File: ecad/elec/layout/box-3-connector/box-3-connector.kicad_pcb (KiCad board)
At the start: 2 copper layers, 72.5 x 7.9 mm, 2 parts

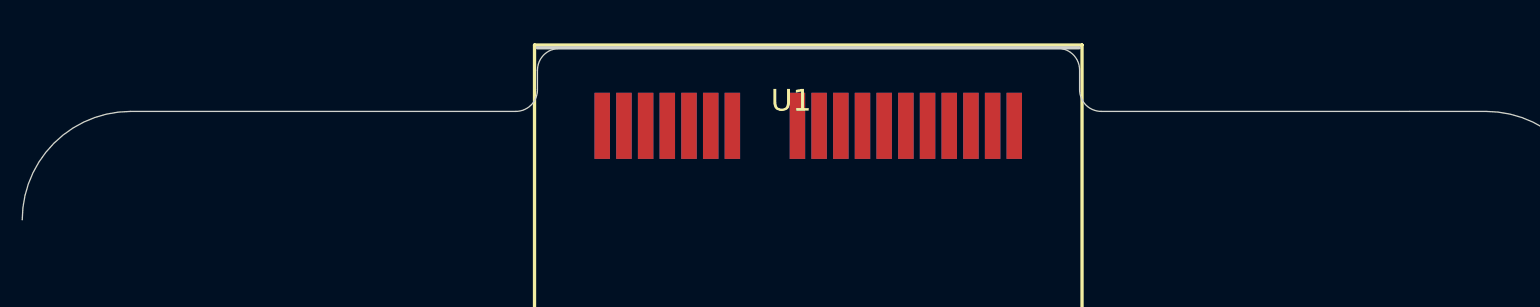
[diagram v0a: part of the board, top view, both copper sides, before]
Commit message: remove default and start fleshing out layouts. fixed issue with fab extending beyond edge cuts in box-3-connector footprint (CONN_5_)
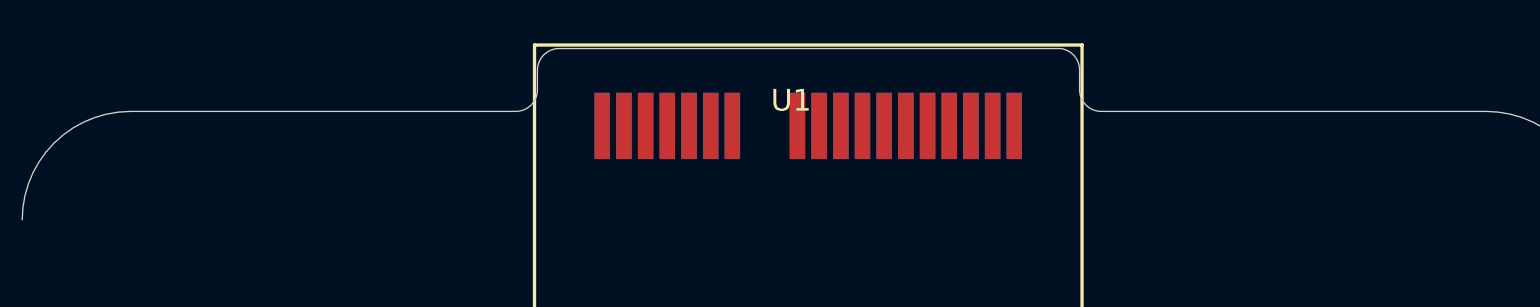
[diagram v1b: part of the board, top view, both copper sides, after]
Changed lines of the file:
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@@
         (effects (font (size 1 1) (thickness 0.15)))
     )
-    (fp_line (start -30.457932 -0.000118) (end -12.700119 -0.000118)
+    (fp_line (start -30.457813 0) (end -12.7 0)
       (stroke (width 0.05) (type solid)) (layer "Edge.Cuts"))
     (fp_line (start -11.699432 -0.999959) (end -11.699432 -1.9)
@@
     (fp_line (start 13.300568 -1.00525) (end 13.300568 -1.9022)
       (stroke (width 0.05) (type solid)) (layer "Edge.Cuts"))
-    (fp_line (start 14.300518 0) (end 28.50595 0)
+    (fp_line (start 14.300516 0) (end 28.505948 0)
       (stroke (width 0.05) (type solid)) (layer "Edge.Cuts"))
     (fp_line (start 32.04209 0.00015) (end 28.5061 0.00015)
@@
     (fp_line (start 12.6238 3.727) (end 12.6238 -13.1386)
       (stroke (width 0.1524) (type solid)) (layer "F.SilkS"))
-    (fp_line (start -12.4968 3.6) (end 12.4968 3.6)
-      (stroke (width 0.1524) (type solid)) (layer "Edge.Cuts"))
-    (fp_line (start -12.4968 -13.0116) (end -12.4968 3.6)
-      (stroke (width 0.1524) (type solid)) (layer "F.Fab"))
-    (fp_line (start -12.4968 3.6) (end 12.4968 3.6)
-      (stroke (width 0.1524) (type solid)) (layer "F.Fab"))
-    (fp_line (start 12.4968 -13.0116) (end -12.4968 -13.0116)
-      (stroke (width 0.1524) (type solid)) (layer "F.Fab"))
-    (fp_line (start 12.4968 3.6) (end 12.4968 -13.0116)
-      (stroke (width 0.1524) (type solid)) (layer "F.Fab"))
     (pad "A1" smd rect (at -9.5 0 270) (size 3.048 0.7112) (layers "F.Cu" "F.Paste" "F.Mask")
       (net 1 "io10") (pintype "stereo") (solder_mask_margin 0.1016) (thermal_bridge_angle 0))

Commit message: update layouts
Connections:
- net cc4484681-gnd renamed conn-gnd

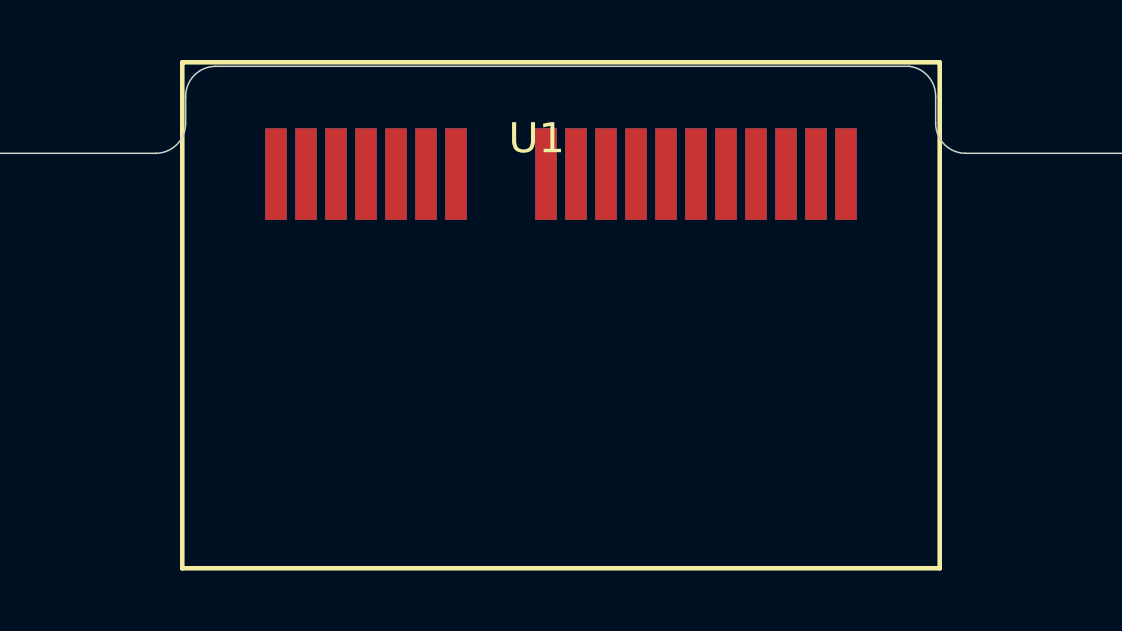
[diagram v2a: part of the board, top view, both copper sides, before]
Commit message: change drv2605 to tssop and update box-3 connector. flesh out implemenation and wiring
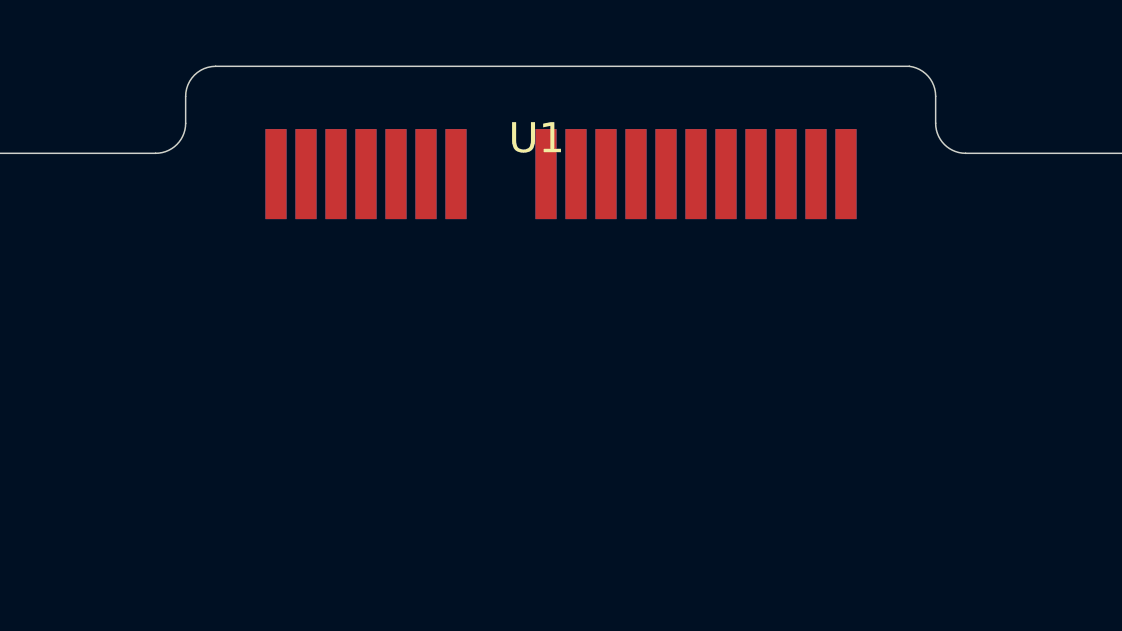
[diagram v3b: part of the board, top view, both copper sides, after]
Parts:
- U2: footprint lib:CONN_5-1734857-1_TEC -> lib:CONN-SMD_5-1734857-1; moved to B.Cu
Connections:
- net _a17 renamed conn-vcc
- net _a18 renamed conn-vcc-1
- net _b7 renamed dm
- net _b8 renamed dp
- U2 pad A13: (no net) -> net
- U2 pad A15: (no net) -> net-1
- U2 pad B13: (no net) -> net-2
- U2 pad B15: (no net) -> net-3

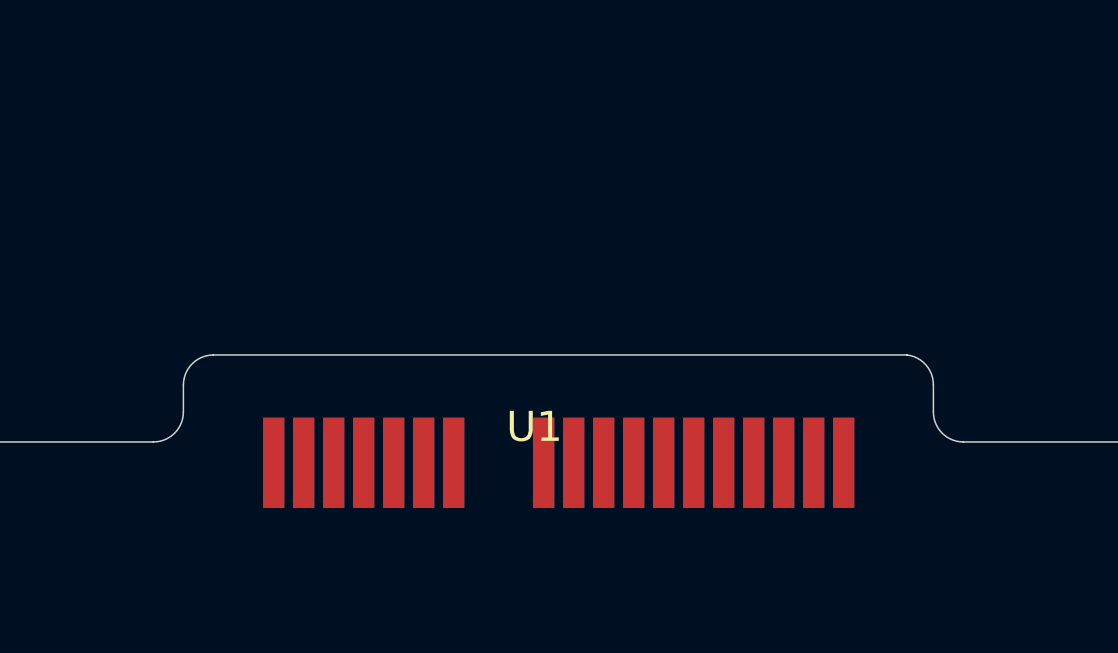
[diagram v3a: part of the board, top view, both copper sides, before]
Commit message: fix box-3 connector pin configuration (lcsc / easyeda model was wrong). updated associated layouts
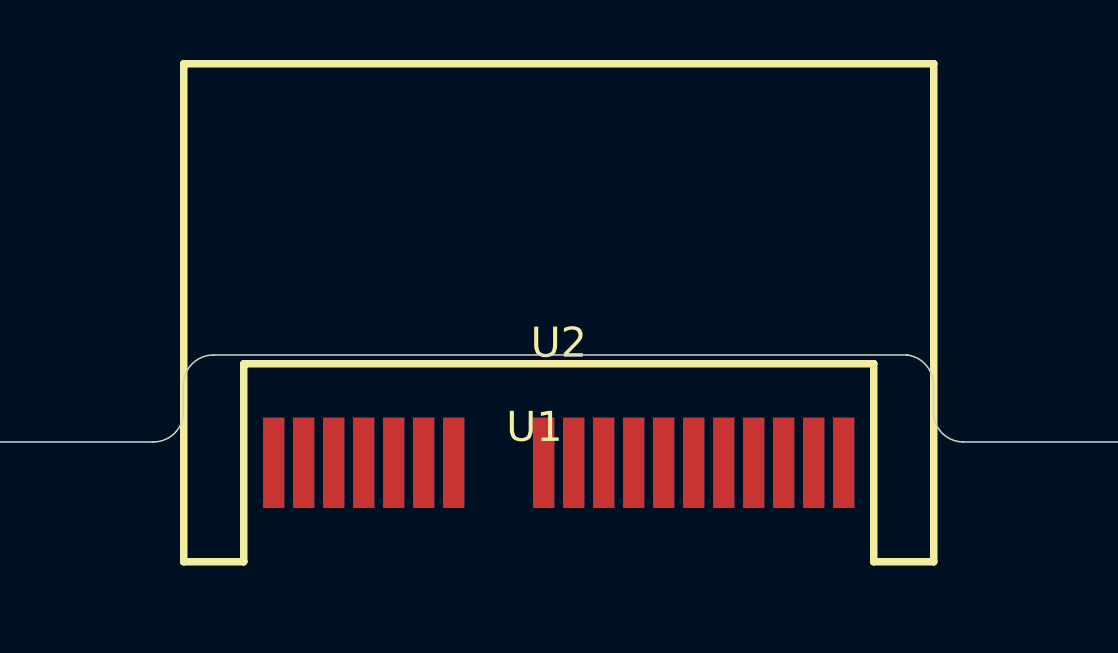
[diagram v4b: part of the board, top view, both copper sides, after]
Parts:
- U2: moved to F.Cu
- turned U2 to 0 degrees
